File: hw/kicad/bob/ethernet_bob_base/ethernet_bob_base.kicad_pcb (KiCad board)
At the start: 2 copper layers, 26 parts, among them J1 DB9_Male, J2 Conn_01x02_Male, P1 CONN_02X25, P2 CONN_02X25, U1 LM5017MR, U2 TJA1021T, U3 MCP2551-I-SN, U4 MC33879A, U5 MC33879A

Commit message: add outputs
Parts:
- added C10: 20µ, Capacitors_SMD:CP_Elec_6.3x7.7, F.Cu at (148.3, 136.5)
- added C11: 20µ, Capacitors_SMD:CP_Elec_6.3x7.7, F.Cu at (167.3, 136.3)
- added J3: Conn_01x02_Male, stmbl-kicad-lib:RM3.5_1x2_UP, F.Cu at (148.3, 161.5)
- added J4: Conn_01x02_Male, stmbl-kicad-lib:RM3.5_1x2_UP, F.Cu at (164.8, 161.3)
- added J5: Conn_01x06_Male, stmbl-kicad-lib:RM3.5_1x6_UP, F.Cu at (125.4, 161.5)
- added J6: Conn_01x06_Male, stmbl-kicad-lib:RM3.5_1x6_UP, F.Cu at (173.7, 161.4)
- added JP1: SolderJumper_3_Bridged12, stmbl-kicad-lib:SOLDER_JUMPER_3_NC, F.Cu at (178.2, 130.5)
- added JP2: SolderJumper_3_Bridged12, stmbl-kicad-lib:SOLDER_JUMPER_3_NC, F.Cu at (176.1, 130.5)
- moved C7 69.3 mm to (172.8, 98.6), turned to 180 degrees
- moved C1 56.2 mm to (168.1, 120.7), turned to 180 degrees
- moved U5 8.51 mm to (169.5, 145.8), turned to 180 degrees
- moved C9 7.70 mm to (165.4, 111.6)
- moved R4 7.70 mm to (171.1, 115.1)
- moved C5 7.70 mm to (172.6, 105.2)
- moved C6 7.70 mm to (169.7, 105.3)
- moved C8 7.70 mm to (167.0, 111.6)
- moved R3 7.70 mm to (173.5, 115.1)
- moved U1 7.70 mm to (170.9, 109.7)
- moved R2 7.70 mm to (171.1, 114.0)
- moved C2 7.70 mm to (168.0, 114.3)
- moved C3 7.70 mm to (168.0, 116.0)
- moved C4 7.70 mm to (173.5, 114.0)
- moved L1 7.70 mm to (166.2, 108.1)
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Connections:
- net Net-(U4-Pad32) renamed /HSDRV_DO
- net PE0 renamed LIN_RX
- net PE1 renamed LIN_TX
- U4 pad 11: Net-(U4-Pad11) -> VD
- U4 pad 12: Net-(U4-Pad12) -> Net-(J3-Pad2)
- U4 pad 21: Net-(U4-Pad21) -> Net-(J3-Pad1)
- U4 pad 22: Net-(U4-Pad22) -> VD
- U4 pad 23: Net-(U4-Pad23) -> Net-(J3-Pad2)
- U4 pad 26: Net-(U4-Pad26) -> VD
- U4 pad 27: Net-(U4-Pad27) -> Net-(J3-Pad1)
- U4 pad 28: Net-(U4-Pad28) -> VD
- U4 pad 31: Net-(U4-Pad31) -> VD
- U4 pad 5: Net-(U4-Pad5) -> VD
- U4 pad 7: Net-(U4-Pad7) -> VD
- U5 pad 11: Net-(U5-Pad11) -> VD
- U5 pad 12: Net-(U5-Pad12) -> Net-(J4-Pad2)
- U5 pad 21: Net-(U5-Pad21) -> Net-(J4-Pad1)
- U5 pad 22: Net-(U5-Pad22) -> VD
- U5 pad 23: Net-(U5-Pad23) -> Net-(J4-Pad2)
- U5 pad 26: Net-(U5-Pad26) -> VD
- U5 pad 27: Net-(U5-Pad27) -> Net-(J4-Pad1)
- U5 pad 28: Net-(U5-Pad28) -> VD
- U5 pad 31: Net-(U5-Pad31) -> VD
- U5 pad 5: Net-(U5-Pad5) -> VD
- U5 pad 7: Net-(U5-Pad7) -> VD
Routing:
- net /psu/SW: track 1.67 -> 4.50 mm
- added copper zone on F.Cu, net +5V

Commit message: routing
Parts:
- added C12: 100n, stmbl:C_0805, F.Cu at (89.4, 79.4)
- added C13: 100n, stmbl:C_0805, F.Cu at (105.9, 119.1)
- added C14: 100n, stmbl:C_0805, F.Cu at (118.6, 72.6)
- added C15: 100n, stmbl:C_0805, F.Cu at (82.7, 118.4)
- added C16: 100n, stmbl:C_0805, F.Cu at (102.5, 90.0)
- added C17: 100n, stmbl:C_0805, F.Cu at (102.5, 92.7)
- added J7: Conn_01x04_Male, stmbl-kicad-lib:RM3.5_1x4_UP, F.Cu at (63.8, 110.2)
- added J8: Conn_01x04_Male, stmbl-kicad-lib:RM3.5_1x4_UP, F.Cu at (63.8, 126.9)
- J5, J6: value Conn_01x06_Male -> Conn_01x04_Male; footprint stmbl-kicad-lib:RM3.5_1x6_UP -> stmbl-kicad-lib:RM3.5_1x4_UP
- moved J6 68.6 mm to (108.0, 141.7)
- moved R1 64.5 mm to (89.5, 68.0), turned to 90 degrees
- moved U2 63.7 mm to (111.6, 70.7)
- moved TP1 63.5 mm to (116.7, 68.8)
- moved C10 60.7 mm to (91.0, 116.5)
- moved J2 58.5 mm to (119.0, 61.3)
- moved P2 58.5 mm to (126.0, 71.3)
- moved R6 58.5 mm to (116.4, 83.6)
- moved U1 58.5 mm to (115.9, 89.7)
- moved C2 58.5 mm to (113.0, 94.3)
- moved C3 58.5 mm to (113.0, 96.0)
- moved C4 58.5 mm to (118.5, 94.0)
- moved C5 58.5 mm to (117.6, 85.2)
- moved C6 58.5 mm to (114.7, 85.3)
- moved C8 58.5 mm to (112.0, 91.6)
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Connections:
- P1 pad 34: PB10 -> HSDRV_SCLK
- P1 pad 39: PB15 -> HSDRV_DI
- P1 pad 46: PD14 -> HSDRV_CS
- P1 pad 47: PD15 -> HSDRV_EN
- P2 pad 17: LIN_RX -> LIN_RXD
- P2 pad 18: LIN_TX -> LIN_TXD
- P2 pad 3: +5VP -> +5V
- P2 pad 4: +5VP -> +5V
- U4 pad 10: Net-(J5-Pad6) -> Net-(J5-Pad3)
- U4 pad 13: Net-(J5-Pad3) -> GND
- U4 pad 14: PWM1 -> PD11
- U4 pad 19: PWM0 -> PD12
- U4 pad 20: Net-(J5-Pad4) -> GND
- U4 pad 29: Net-(J5-Pad2) -> Net-(J5-Pad4)
- U4 pad 6: Net-(J5-Pad5) -> Net-(J5-Pad2)
- U5 pad 10: Net-(J6-Pad1) -> Net-(J6-Pad3)
- U5 pad 13: Net-(J6-Pad4) -> GND
- U5 pad 14: PWM3 -> PC7
- U5 pad 19: PWM2 -> PC6
- U5 pad 20: Net-(J6-Pad3) -> GND
- U5 pad 29: Net-(J6-Pad5) -> Net-(J6-Pad4)
- U5 pad 3: Net-(J6-Pad6) -> Net-(J6-Pad1)
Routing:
- net +3V3: track 0.00 -> 127.8 mm, vias 0 -> 1
- net HSDRV_SCLK: track 0.00 -> 61.4 mm, vias 0 -> 5
- net HSDRV_CS: track 0.00 -> 50.0 mm, vias 0 -> 4
- net HSDRV_EN: track 0.00 -> 42.4 mm, vias 0 -> 4
- net HSDRV_DI: track 0.00 -> 41.7 mm, vias 0 -> 2
- net Net-(J3-Pad2): track 0.00 -> 40.7 mm, vias 0 -> 2
- net Net-(J4-Pad2): track 0.00 -> 38.8 mm, vias 0 -> 3
- net LIN_TXD: track 0.00 -> 37.6 mm, vias 0 -> 1
- net /HSDRV_DO: track 0.00 -> 37.4 mm, vias 0 -> 2
- net LIN_RXD: track 0.00 -> 31.5 mm, vias 0 -> 1
- net Net-(J5-Pad4): track 0.00 -> 27.0 mm
- net Net-(J4-Pad1): track 0.00 -> 24.8 mm, vias 0 -> 1
- net Net-(J6-Pad3): track 0.00 -> 24.4 mm
- net Net-(J6-Pad4): track 0.00 -> 24.1 mm
- net PD12: track 0.00 -> 24.0 mm, vias 0 -> 1
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- added copper zone on B.Cu, net GND
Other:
- board outline added: 65 x 100 mm
- net class Output added: clearance 0.125, trace_width 0.5, via_dia 0.8, via_drill 0.4

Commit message: routing...
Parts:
- added C18: C, stmbl-kicad-lib:C_0805, F.Cu at (72.5, 77.5)
- added C19: C, stmbl-kicad-lib:C_0805, F.Cu at (72.5, 94.0)
- added C20: C, stmbl-kicad-lib:C_0805, F.Cu at (131.8, 88.0)
- added C21: C, stmbl-kicad-lib:C_0805, F.Cu at (131.8, 104.5)
- added C22: C, stmbl-kicad-lib:C_0805, F.Cu at (72.5, 81.0)
- added C23: C, stmbl-kicad-lib:C_0805, F.Cu at (72.5, 97.5)
- added C24: C, stmbl-kicad-lib:C_0805, F.Cu at (131.8, 84.5)
- added C25: C, stmbl-kicad-lib:C_0805, F.Cu at (131.8, 101.0)
- added C26: C, stmbl-kicad-lib:C_0805, F.Cu at (72.5, 84.5)
- added C27: C, stmbl-kicad-lib:C_0805, F.Cu at (72.5, 101.0)
- added C28: C, stmbl-kicad-lib:C_0805, F.Cu at (131.8, 81.0)
- added C29: C, stmbl-kicad-lib:C_0805, F.Cu at (131.8, 97.5)
- added C30: C, stmbl-kicad-lib:C_0805, F.Cu at (72.5, 88.0)
- added C31: C, stmbl-kicad-lib:C_0805, F.Cu at (72.5, 104.5)
- added C32: C, stmbl-kicad-lib:C_0805, F.Cu at (131.8, 77.5)
- added C33: C, stmbl-kicad-lib:C_0805, F.Cu at (131.8, 94.0)
- added H1: MountingHole_Pad, Mounting_Holes:MountingHole_3.2mm_M3_Pad_Via, F.Cu at (54.0, 54.0)
- added H2: MountingHole_Pad, Mounting_Holes:MountingHole_3.2mm_M3_Pad_Via, F.Cu at (146.0, 146.0)
- added H3: MountingHole_Pad, Mounting_Holes:MountingHole_3.2mm_M3_Pad_Via, F.Cu at (146.0, 54.0)
- added H4: MountingHole_Pad, Mounting_Holes:MountingHole_3.2mm_M3_Pad_Via, F.Cu at (54.0, 146.0)
- added J10: Conn_01x04_Male, stmbl-kicad-lib:RM3.5_1x4_UP, F.Cu at (63.0, 93.0)
- added J11: Conn_01x04_Male, stmbl-kicad-lib:RM3.5_1x4_UP, F.Cu at (141.2, 87.0)
- added J12: Conn_01x04_Male, stmbl-kicad-lib:RM3.5_1x4_UP, F.Cu at (141.2, 103.5)
- added J9: Conn_01x04_Male, stmbl-kicad-lib:RM3.5_1x4_UP, F.Cu at (63.0, 76.5)
- added R10: R, stmbl-kicad-lib:R_0603, F.Cu at (68.8, 87.0)
- added R11: R, stmbl-kicad-lib:R_0603, F.Cu at (68.8, 93.0)
- added R12: R, stmbl-kicad-lib:R_0603, F.Cu at (68.8, 96.5)
- added R13: R, stmbl-kicad-lib:R_0603, F.Cu at (68.8, 100.0)
- added R14: R, stmbl-kicad-lib:R_0603, F.Cu at (68.8, 103.5)
- added R15: R, stmbl-kicad-lib:R_0603, F.Cu at (135.5, 87.0)
- added R16: R, stmbl-kicad-lib:R_0603, F.Cu at (135.5, 83.5)
- added R17: R, stmbl-kicad-lib:R_0603, F.Cu at (135.5, 80.0)
- added R18: R, stmbl-kicad-lib:R_0603, F.Cu at (135.5, 76.5)
- added R19: R, stmbl-kicad-lib:R_0603, F.Cu at (135.5, 103.5)
- added R20: R, stmbl-kicad-lib:R_0603, F.Cu at (135.5, 100.0)
- added R21: R, stmbl-kicad-lib:R_0603, F.Cu at (135.5, 96.5)
- added R22: R, stmbl-kicad-lib:R_0603, F.Cu at (135.5, 93.0)
- added R23: R, stmbl-kicad-lib:R_0603, F.Cu at (70.2, 77.8)
- added R24: R, stmbl-kicad-lib:R_0603, F.Cu at (70.2, 94.2)
- added R25: R, stmbl-kicad-lib:R_0603, F.Cu at (134.0, 88.2)
- added R26: R, stmbl-kicad-lib:R_0603, F.Cu at (134.0, 104.8)
- added R27: R, stmbl-kicad-lib:R_0603, F.Cu at (70.2, 81.2)
- added R28: R, stmbl-kicad-lib:R_0603, F.Cu at (70.2, 97.8)
- added R29: R, stmbl-kicad-lib:R_0603, F.Cu at (134.0, 84.8)
- added R30: R, stmbl-kicad-lib:R_0603, F.Cu at (134.0, 101.2)
- added R31: R, stmbl-kicad-lib:R_0603, F.Cu at (70.2, 84.8)
- added R32: R, stmbl-kicad-lib:R_0603, F.Cu at (70.2, 101.2)
- added R33: R, stmbl-kicad-lib:R_0603, F.Cu at (134.0, 81.2)
- added R34: R, stmbl-kicad-lib:R_0603, F.Cu at (134.0, 97.8)
- added R35: R, stmbl-kicad-lib:R_0603, F.Cu at (70.2, 88.2)
- added R36: R, stmbl-kicad-lib:R_0603, F.Cu at (70.2, 104.8)
- added R37: R, stmbl-kicad-lib:R_0603, F.Cu at (134.0, 77.8)
- added R38: R, stmbl-kicad-lib:R_0603, F.Cu at (134.0, 94.2)
- added R7: R, stmbl-kicad-lib:R_0603, F.Cu at (68.8, 76.5)
- added R8: R, stmbl-kicad-lib:R_0603, F.Cu at (68.8, 80.0)
- added R9: R, stmbl-kicad-lib:R_0603, F.Cu at (68.8, 83.5)
- moved J8 0.76 mm to (63.0, 127.0)
- moved J7 0.75 mm to (63.0, 110.2)
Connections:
- P1 pad 10: PC2 -> ADC1
- P1 pad 12: PA0 -> ADC3
- P1 pad 15: PA5 -> ADC4
- P1 pad 16: PA4 -> ADC5
- P1 pad 18: PA6 -> ADC6
- P1 pad 21: PB1 -> ADC7
- P1 pad 8: PC0 -> ADC0
- P1 pad 9: PC3 -> ADC2
- P2 pad 10: PC15 -> ADC10
- P2 pad 12: PC13 -> ADC9
- P2 pad 14: PE5 -> ADC8
- P2 pad 20: PB9 -> ADC15
- P2 pad 24: PB7 -> ADC14
- P2 pad 25: PB4 -> ADC13
- P2 pad 28: PB3 -> ADC12
- P2 pad 9: PC14 -> ADC11
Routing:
- net ADC6: track 0.00 -> 15.4 mm
- net ADC5: track 0.00 -> 14.3 mm
- net ADC7: track 0.00 -> 13.6 mm
- net ADC11: track 0.00 -> 12.6 mm
- net ADC13: track 0.00 -> 10.7 mm
- net ADC3: track 0.00 -> 10.5 mm
- net ADC0: track 0.00 -> 10.3 mm
- net ADC1: track 0.00 -> 9.92 mm
- net ADC4: track 0.00 -> 9.16 mm
- net ADC14: track 0.00 -> 8.93 mm
- net ADC10: track 0.00 -> 8.04 mm
- net ADC15: track 0.00 -> 7.91 mm
- net ADC12: track 0.00 -> 7.77 mm
- net ADC9: track 0.00 -> 7.64 mm
- net ADC8: track 0.00 -> 7.58 mm
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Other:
- board size 65 x 100 mm -> 100 x 100 mm

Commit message: RC0?
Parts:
- removed C16, C17: 100n, stmbl:C_0805
- moved JP1 2.14 mm to (122.5, 112.5), turned to 180 degrees
- moved JP2 1.73 mm to (122.5, 109.5), turned to 180 degrees
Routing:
- net VD: track 0.00 -> 103.0 mm, vias 0 -> 5
- net CAN_TXD: track 0.00 -> 63.1 mm
- net CAN_RXD: track 0.00 -> 56.2 mm
- net PB5: track 9.67 -> 17.8 mm, vias 0 -> 2
- net PD0: track 0.00 -> 4.98 mm
- net PD1: track 0.00 -> 3.47 mm
- net PB6: track 11.3 -> 11.8 mm
- net GND: vias 48 -> 52

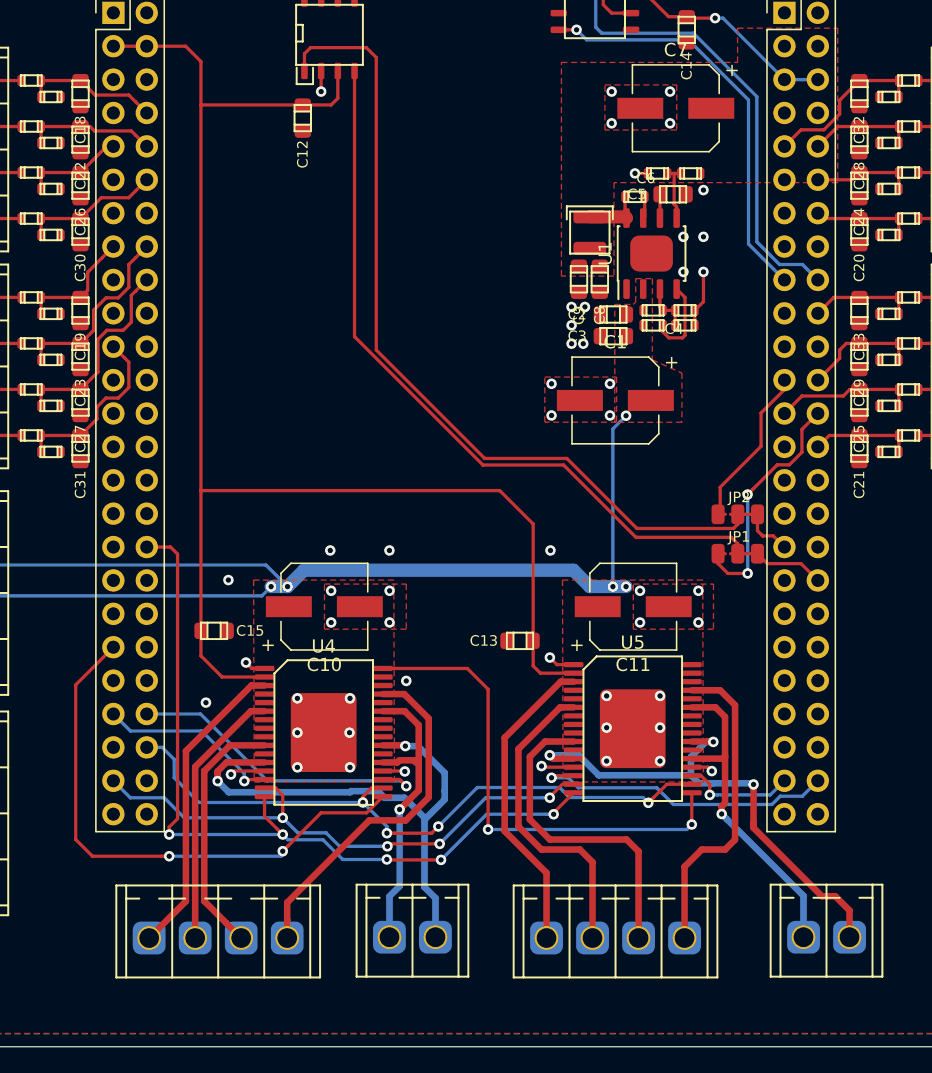
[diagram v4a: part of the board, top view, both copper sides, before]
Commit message: add leds
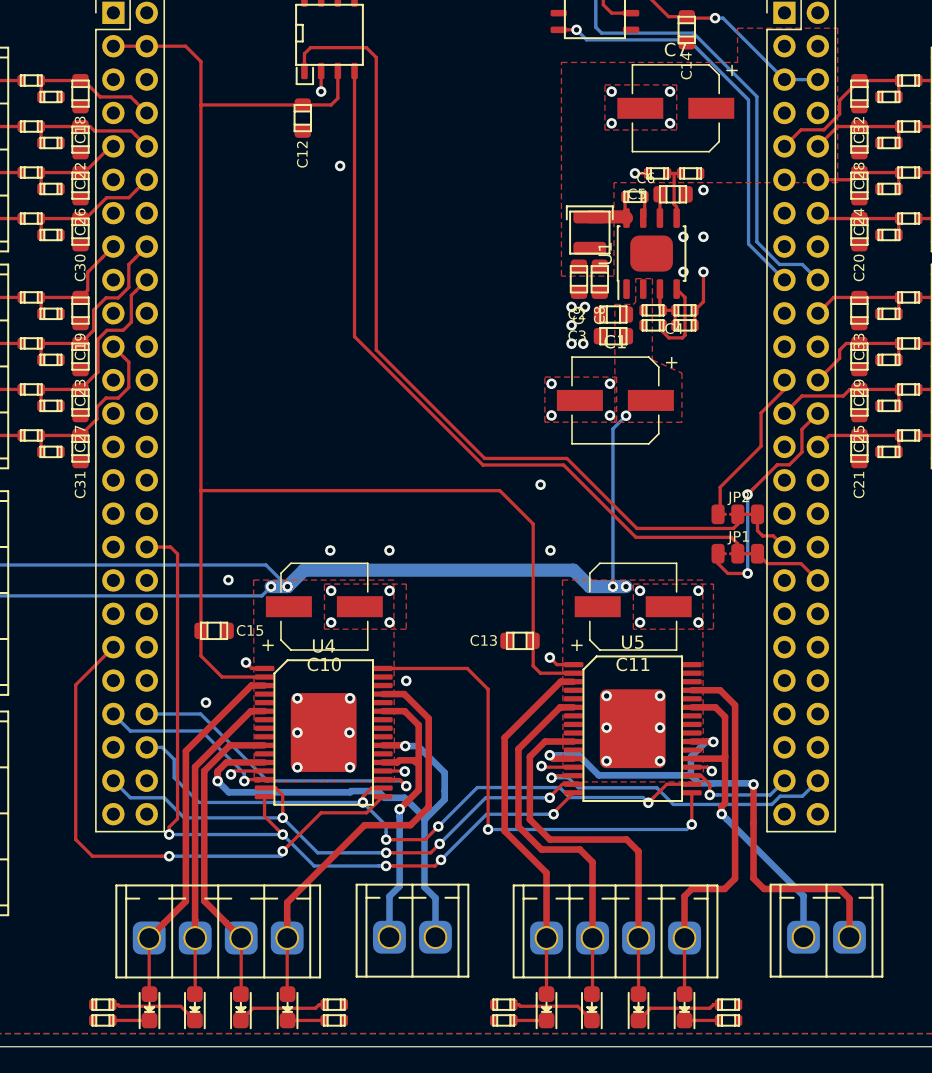
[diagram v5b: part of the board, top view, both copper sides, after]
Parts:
- added D1: LED, stmbl-kicad-lib:LED-0805, F.Cu at (108.0, 147.0)
- added D2: LED, stmbl-kicad-lib:LED-0805, F.Cu at (77.8, 147.0)
- added D3: LED, stmbl-kicad-lib:LED-0805, F.Cu at (118.5, 147.0)
- added D4: LED, stmbl-kicad-lib:LED-0805, F.Cu at (88.2, 147.0)
- added D5: LED, stmbl-kicad-lib:LED-0805, F.Cu at (111.4, 147.0)
- added D6: LED, stmbl-kicad-lib:LED-0805, F.Cu at (81.2, 147.0)
- added D7: LED, stmbl-kicad-lib:LED-0805, F.Cu at (115.0, 147.0)
- added D8: LED, stmbl-kicad-lib:LED-0805, F.Cu at (84.7, 147.0)
- added R39: R, stmbl-kicad-lib:R_0603, F.Cu at (104.7, 148.0)
- added R40: R, stmbl-kicad-lib:R_0603, F.Cu at (74.2, 148.0)
- added R41: R, stmbl-kicad-lib:R_0603, F.Cu at (121.8, 148.0)
- added R42: R, stmbl-kicad-lib:R_0603, F.Cu at (91.8, 148.0)
- added R43: R, stmbl-kicad-lib:R_0603, F.Cu at (104.7, 146.8)
- added R44: R, stmbl-kicad-lib:R_0603, F.Cu at (74.2, 146.8)
- added R45: R, stmbl-kicad-lib:R_0603, F.Cu at (121.8, 146.8)
- added R46: R, stmbl-kicad-lib:R_0603, F.Cu at (91.8, 146.8)
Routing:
- net Net-(D8-Pad1): track 0.00 -> 6.85 mm
- net Net-(D6-Pad1): track 0.00 -> 6.75 mm
- net Net-(D7-Pad1): track 0.00 -> 6.60 mm
- net Net-(D5-Pad1): track 0.00 -> 6.45 mm
- net Net-(D4-Pad2): track 27.0 -> 31.7 mm
- net Net-(D3-Pad2): track 24.1 -> 28.8 mm
- net Net-(D5-Pad2): track 23.9 -> 28.2 mm
- net Net-(D6-Pad2): track 20.1 -> 24.3 mm
- net Net-(D2-Pad2): track 23.4 -> 27.7 mm
- net Net-(D8-Pad2): track 19.3 -> 23.5 mm
- net Net-(D7-Pad2): track 24.4 -> 28.7 mm
- net Net-(D1-Pad2): track 23.6 -> 27.8 mm
- net Net-(D4-Pad1): track 0.00 -> 2.80 mm
- net Net-(D2-Pad1): track 0.00 -> 2.80 mm
- net Net-(J4-Pad2): track 38.8 -> 41.6 mm
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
